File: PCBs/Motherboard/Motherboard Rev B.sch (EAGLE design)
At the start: 52 parts, among them J2 MOLEX_504050-0491, Q1 32kHZ, U1 Value, X1 2514-5

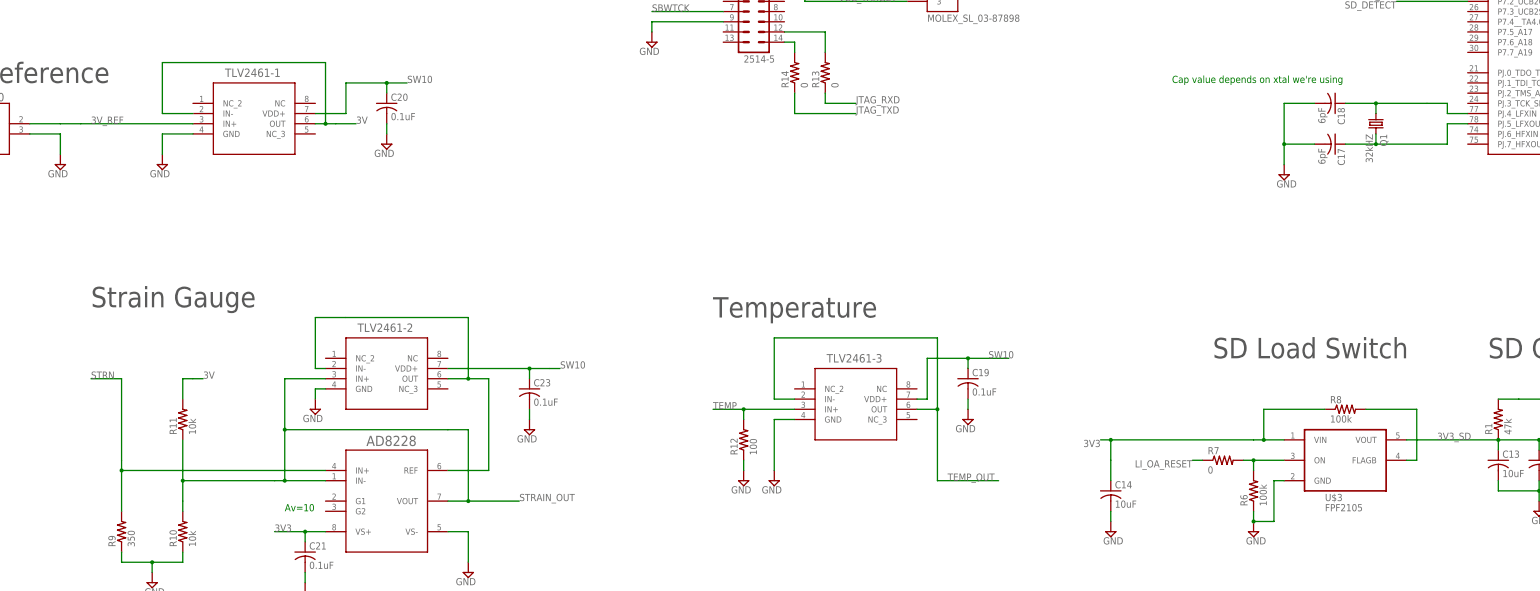
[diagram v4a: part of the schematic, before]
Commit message: Add HFXtal
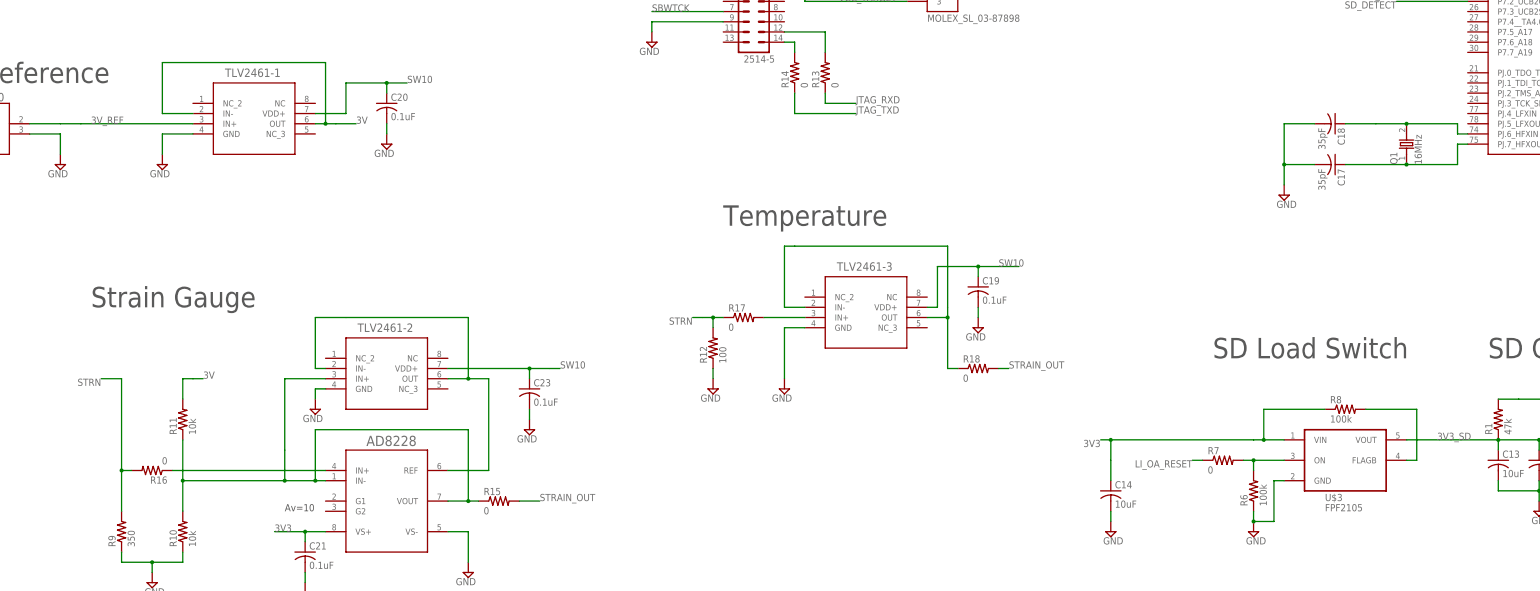
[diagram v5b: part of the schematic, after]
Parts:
- added R15, R16, R17, R18: 0, resistor:R-US_R0805
- C17, C18: value 6pF -> 35pF
- Q1: value 32kHZ -> 16MHz; device crystal:CRYSTALHC49S -> C5BQ:FOX-C5BQ
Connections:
- new net N$12: C18.1, Q1.2, U1.PJ.6_HFXIN
- new net N$13: R17.2, TLV2461-3.IN+
- new net N$14: AD8228.IN-, AD8228.VOUT, R10.2, R11.1, R15.1, TLV2461-2.IN+
- new net N$16: R18.1, TLV2461-3.IN-, TLV2461-3.OUT
- net N$4: now also Q1.1, U1.PJ.7_HFXOUT; no longer Q1.2, U1.PJ.5_LFXOUT
- net N$6: now also AD8228.IN+, R16.1; no longer C18.1, Q1.1, U1.PJ.4_LFXIN
- net STRAIN_OUT: now also R15.2, R18.2; no longer AD8228.IN-, AD8228.VOUT, R10.2, R11.1, TLV2461-2.IN+
- net STRN: now also R12.2, R16.2, R17.1; no longer AD8228.IN+
- net TEMP: no longer R12.2, TLV2461-3.IN+
- net TEMP_OUT: no longer TLV2461-3.IN-, TLV2461-3.OUT
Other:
- note removed: "Cap value depends on xtal we're using"
- moved on the sheet: C17, C18, C19, R12, TLV2461-3

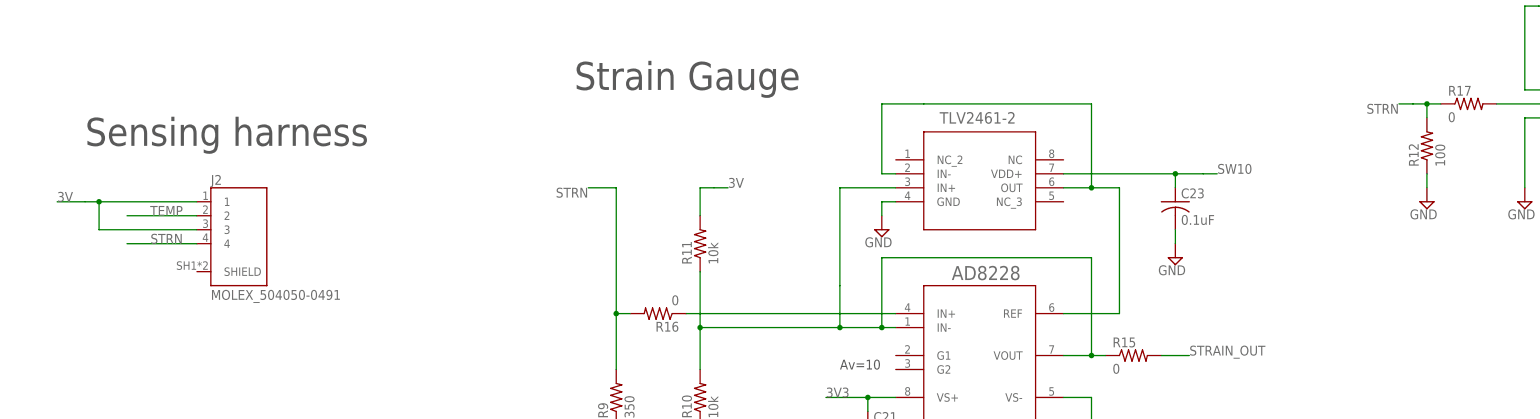
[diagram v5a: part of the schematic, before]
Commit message: Use 5-pin Pico-Lock for sensor harness
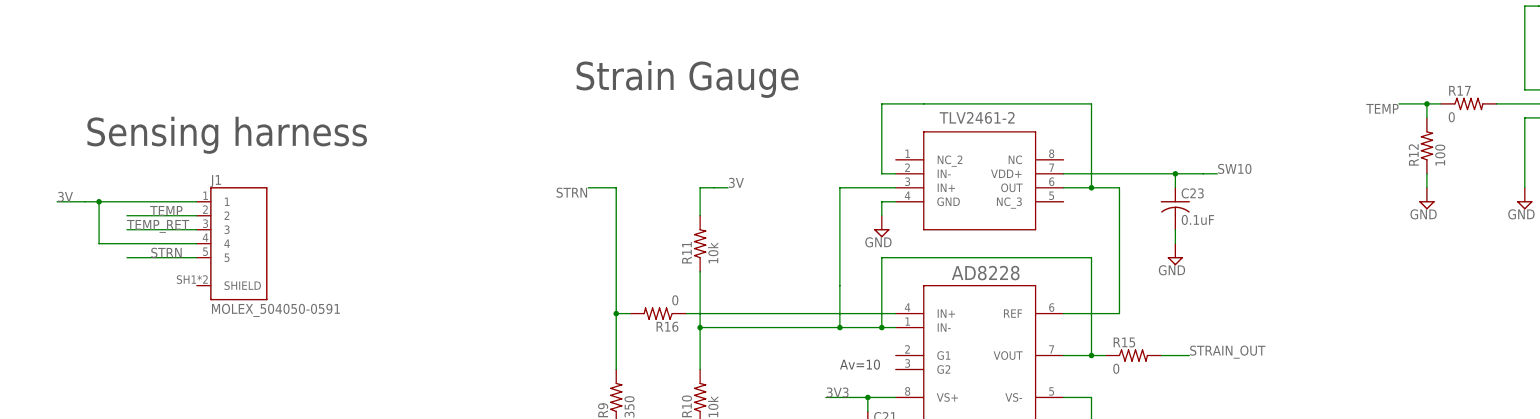
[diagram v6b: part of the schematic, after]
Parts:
- removed J2: MOLEX_504050-0491, Molex 504050-0491:MOLEX_504050-0491
- added J1: MOLEX_504050-0591, Molex 504050:MOLEX_504050-0591
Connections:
- new net TEMP_RET: J1.3
- net 3V: now also J1.1, J1.4; no longer J2.1, J2.3
- net STRN: now also J1.5; no longer J2.4, R12.2, R17.1
- net TEMP: now also J1.2, R12.2, R17.1; no longer J2.2
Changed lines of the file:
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@@
 <part name="R11" library="resistor" library_urn="urn:adsk.eagle:library:348" deviceset="R-US_" device="R0805" package3d_urn="urn:adsk.eagle:package:23553/2" value="10k"/>
 <part name="SUPPLY25" library="supply2" library_urn="urn:adsk.eagle:library:372" deviceset="GND" device=""/>
-<part name="J2" library="Molex 504050-0491" deviceset="MOLEX_504050-0491" device=""/>
 <part name="REF3330" library="REF3330" deviceset="REF3330_DBZ_3" device=""/>
 <part name="SUPPLY28" library="supply2" library_urn="urn:adsk.eagle:library:372" deviceset="GND" device=""/>
@@
 <part name="R18" library="resistor" library_urn="urn:adsk.eagle:library:348" deviceset="R-US_" device="R0805" package3d_urn="urn:adsk.eagle:package:23553/2" value="0"/>
 <part name="R17" library="resistor" library_urn="urn:adsk.eagle:library:348" deviceset="R-US_" device="R0805" package3d_urn="urn:adsk.eagle:package:23553/2" value="0"/>
+<part name="J1" library="Molex 504050" deviceset="MOLEX_504050-0591" device=""/>
 </parts>
 <sheets>
@@
 <instance part="R11" gate="G$1" x="205.74" y="-55.88" rot="R90"/>
 <instance part="SUPPLY25" gate="GND" x="198.12" y="-96.52"/>
-<instance part="J2" gate="G$1" x="121.92" y="-53.34"/>
 <instance part="REF3330" gate="A" x="139.7" y="17.78" smashed="yes">
 <attribute name="NAME" x="149.86" y="23.368" size="2.0828" layer="95" ratio="6" rot="SR0"/>
@@
 <instance part="R18" gate="G$1" x="403.86" y="-43.18"/>
 <instance part="R17" gate="G$1" x="345.44" y="-30.48"/>
+<instance part="J1" gate="G$1" x="121.92" y="-53.34"/>
 </instances>
 <busses>
@@
 <net name="TEMP" class="0">
 <segment>
-<pinref part="J2" gate="G$1" pin="2"/>
 <wire x1="114.3" y1="-50.8" x2="101.6" y2="-50.8" width="0.1524" layer="91"/>
 <label x="111.76" y="-50.8" size="1.778" layer="95" rot="MR0"/>
+<pinref part="J1" gate="G$1" pin="2"/>
+</segment>
+<segment>
+<pinref part="R17" gate="G$1" pin="1"/>
+<wire x1="340.36" y1="-30.48" x2="337.82" y2="-30.48" width="0.1524" layer="91"/>
+<pinref part="R12" gate="G$1" pin="2"/>
+<wire x1="337.82" y1="-30.48" x2="337.82" y2="-33.02" width="0.1524" layer="91"/>
+<wire x1="337.82" y1="-30.48" x2="332.74" y2="-30.48" width="0.1524" layer="91"/>
+<junction x="337.82" y="-30.48"/>
+<label x="332.74" y="-30.48" size="1.778" layer="95" rot="R180"/>
 </segment>
 </net>
 <net name="STRN" class="0">
 <segment>
-<pinref part="J2" gate="G$1" pin="4"/>
-<wire x1="114.3" y1="-55.88" x2="101.6" y2="-55.88" width="0.1524" layer="91"/>
-<label x="111.76" y="-55.88" size="1.778" layer="95" rot="MR0"/>
-</segment>
-<segment>
-<wire x1="335.28" y1="-30.48" x2="332.74" y2="-30.48" width="0.1524" layer="91"/>
-<label x="332.74" y="-30.48" size="1.778" layer="95" rot="R180"/>
-<pinref part="R12" gate="G$1" pin="2"/>
-<wire x1="335.28" y1="-30.48" x2="337.82" y2="-30.48" width="0.1524" layer="91"/>
-<wire x1="337.82" y1="-30.48" x2="337.82" y2="-33.02" width="0.1524" layer="91"/>
-<pinref part="R17" gate="G$1" pin="1"/>
-<wire x1="337.82" y1="-30.48" x2="340.36" y2="-30.48" width="0.1524" layer="91"/>
-<junction x="337.82" y="-30.48"/>
+<wire x1="114.3" y1="-58.42" x2="101.6" y2="-58.42" width="0.1524" layer="91"/>
+<label x="111.76" y="-58.42" size="1.778" layer="95" rot="MR0"/>
+<pinref part="J1" gate="G$1" pin="5"/>
 </segment>
 <segment>
@@
 <net name="3V" class="0">
 <segment>
-<pinref part="J2" gate="G$1" pin="1"/>
 <wire x1="114.3" y1="-48.26" x2="96.52" y2="-48.26" width="0.1524" layer="91"/>
-<pinref part="J2" gate="G$1" pin="3"/>
-<wire x1="114.3" y1="-53.34" x2="96.52" y2="-53.34" width="0.1524" layer="91"/>
-<wire x1="96.52" y1="-53.34" x2="96.52" y2="-48.26" width="0.1524" layer="91"/>
+<wire x1="114.3" y1="-55.88" x2="96.52" y2="-55.88" width="0.1524" layer="91"/>
+<wire x1="96.52" y1="-55.88" x2="96.52" y2="-48.26" width="0.1524" layer="91"/>
 <wire x1="96.52" y1="-48.26" x2="93.98" y2="-48.26" width="0.1524" layer="91"/>
 <junction x="96.52" y="-48.26"/>
 <label x="88.9" y="-48.26" size="1.778" layer="95"/>
 <wire x1="93.98" y1="-48.26" x2="88.9" y2="-48.26" width="0.1524" layer="91"/>
+<pinref part="J1" gate="G$1" pin="1"/>
+<pinref part="J1" gate="G$1" pin="4"/>
 </segment>
 <segment>
@@
 </segment>
 </net>
+<net name="TEMP_RET" class="0">
+<segment>
+<pinref part="J1" gate="G$1" pin="3"/>
+<wire x1="114.3" y1="-53.34" x2="101.6" y2="-53.34" width="0.1524" layer="91"/>
+<label x="101.6" y="-53.34" size="1.778" layer="95"/>
+</segment>
+</net>

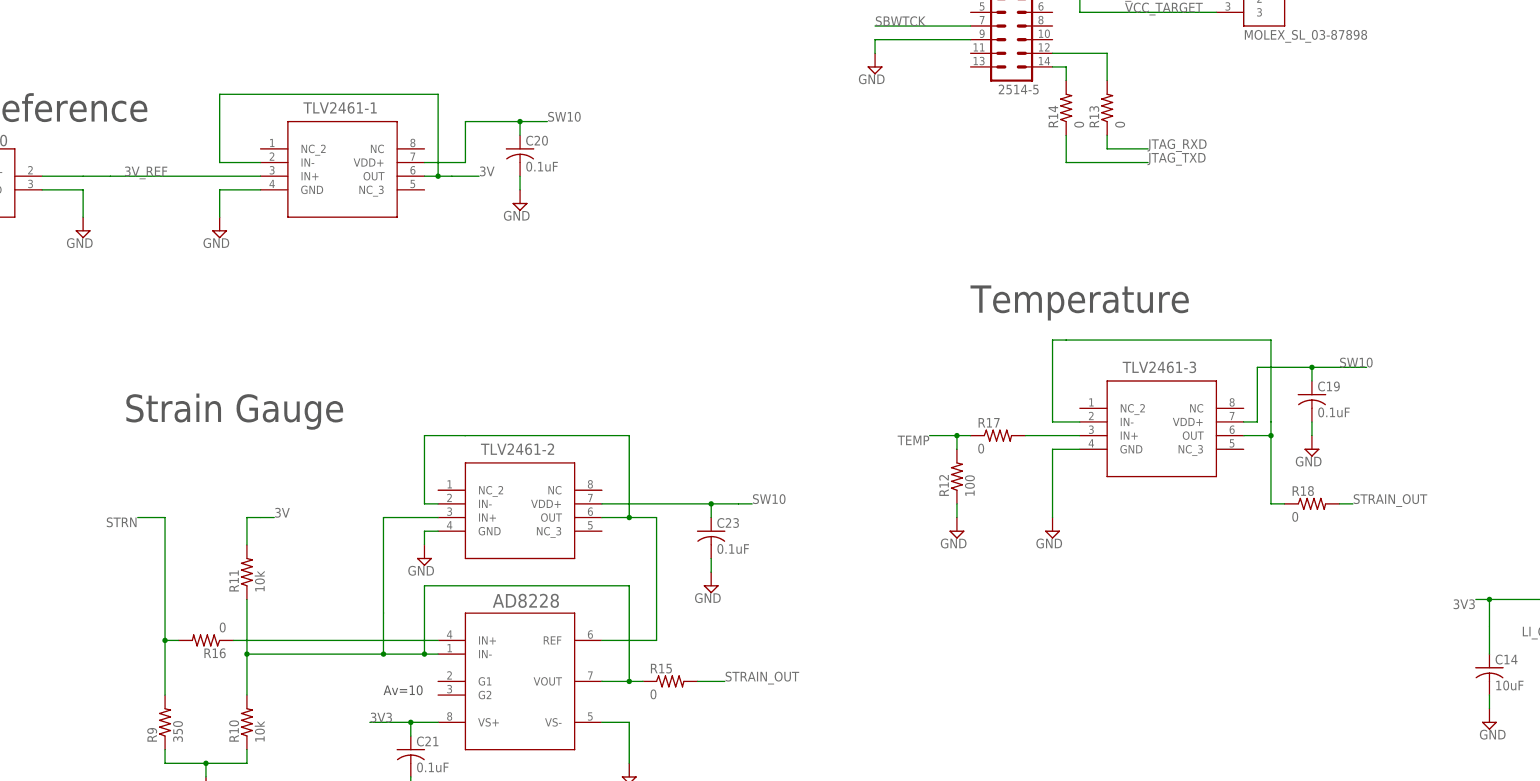
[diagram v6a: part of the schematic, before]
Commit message: Changed opamps used in sensing circuits
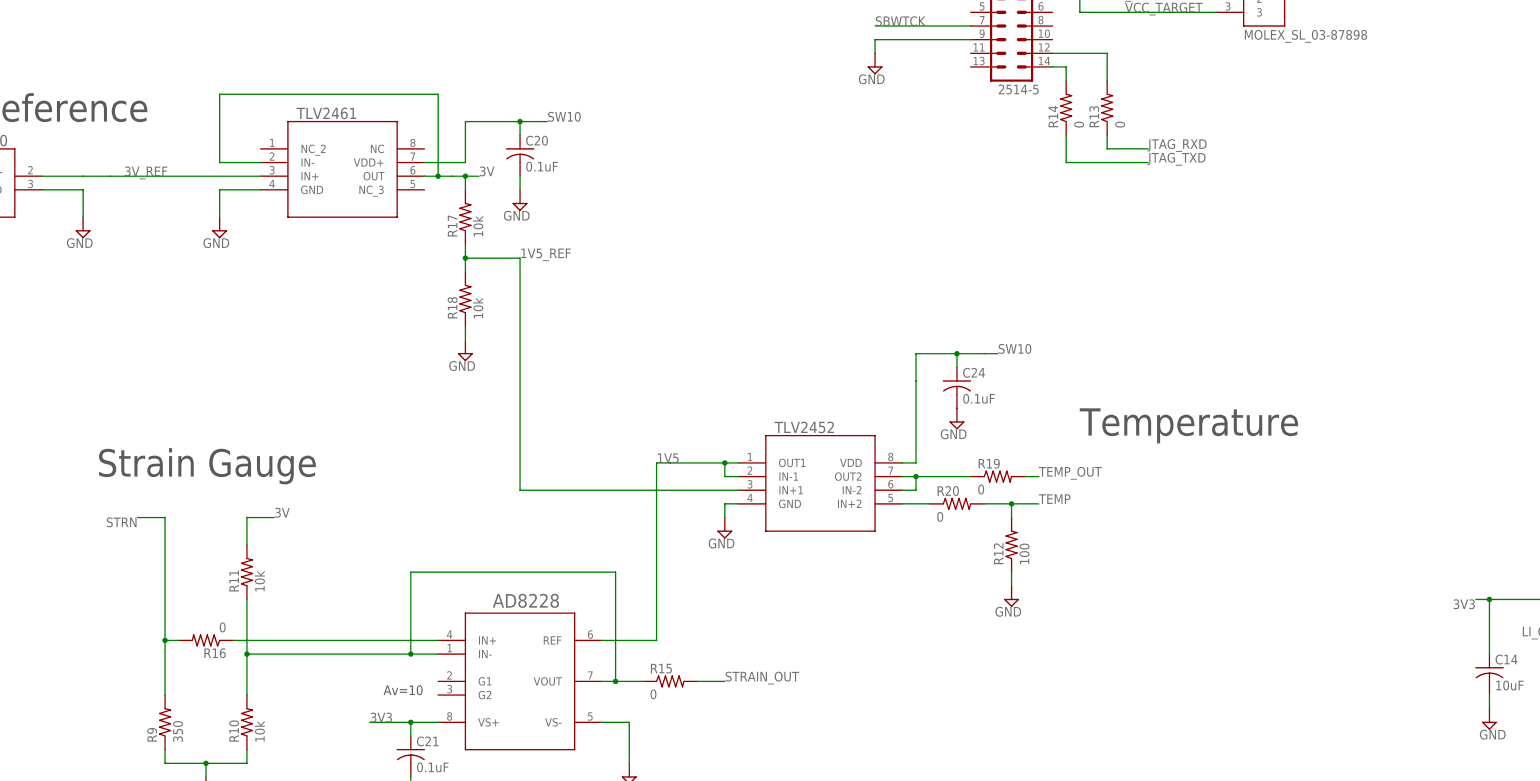
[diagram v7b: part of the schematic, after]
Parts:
- removed C19, C23: 0.1uF, resistor:C-USC0805
- removed TLV2461-1, TLV2461-2, TLV2461-3: TLV2461A_D_8, TLV2461:TLV2461A_D_8
- added C24: 0.1uF, resistor:C-USC0805
- added R19, R20: 0, resistor:R-US_R0805
- added TLV2452: TLV2452, TLV24xx:TLV2452
- added TLV2461: TLV2461A_D_8, TLV24xx:TLV2461A_D_8
- R17, R18: value 0 -> 10k
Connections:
- removed net N$13: R17.2, TLV2461-3.IN+
- removed net N$14: AD8228.IN-, AD8228.VOUT, R10.2, R11.1, R15.1, TLV2461-2.IN+
- removed net N$16: R18.1, TLV2461-3.IN-, TLV2461-3.OUT
- removed net N$9: AD8228.REF, TLV2461-2.IN-, TLV2461-2.OUT
- new net 1V5: AD8228.REF, TLV2452.IN-1, TLV2452.OUT1
- new net 1V5_REF: R17.1, R18.2, TLV2452.IN+1
- new net N$15: R19.1, TLV2452.IN-2, TLV2452.OUT2
- new net N$17: R20.1, TLV2452.IN+2
- net 3V: now also R17.2, TLV2461.IN-, TLV2461.OUT; no longer TLV2461-1.IN-, TLV2461-1.OUT
- net 3V_REF: now also TLV2461.IN+; no longer TLV2461-1.IN+
- net GND: now also C24.2, R18.1, TLV2452.GND, TLV2461.GND; no longer C19.2, C23.2, TLV2461-1.GND, TLV2461-2.GND
- net N$10: now also AD8228.IN-, AD8228.VOUT, R10.2, R11.1, R15.1; no longer TLV2461-3.GND
- net STRAIN_OUT: no longer R18.2
- net SW10: now also C24.1, TLV2452.VDD, TLV2461.VDD+; no longer C19.1, C23.1, TLV2461-1.VDD+, TLV2461-2.VDD+, TLV2461-3.VDD+
- net TEMP: now also R20.2; no longer R17.1
- net TEMP_OUT: now also R19.2
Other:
- moved on the sheet: R12, R17, R18

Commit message: Add xtals, antenna harness, finish most wiring
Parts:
- added C19, C23: 12pF, resistor:C-USC0805
- added J2: MOLEX_504050-0491, Molex 504050-0491:MOLEX_504050-0491
- added Q2: 32.768k, MS1V-T1K:MS1V-T1K
- Q1: value 16MHz -> 16M
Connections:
- removed net 3V1: C14.1
- new net N$13: C19.1, Q2.2, U1.PJ.5_LFXOUT
- new net N$9: C23.1, Q2.1, U1.PJ.4_LFXIN
- net 3V3: now also C14.1; no longer AD8228.VS+, C21.1
- net AGND: now also C17.2, C18.2, C19.2, C23.2
- net GND: now also J2.4; no longer C17.2, C18.2
- net SCL_ANT: now also J2.2
- net SDA_ANT: now also J2.3
- net SW10: now also AD8228.VS+, C21.1
- net SW5: now also J2.1
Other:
- note added: "Antenna"
- moved on the sheet: C17, C18, Q1
